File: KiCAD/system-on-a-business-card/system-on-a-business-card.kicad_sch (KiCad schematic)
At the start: 10 parts, among them J1 USB_C_Receptacle, SW1 SW_Push, U1 USBLC6-2SC6

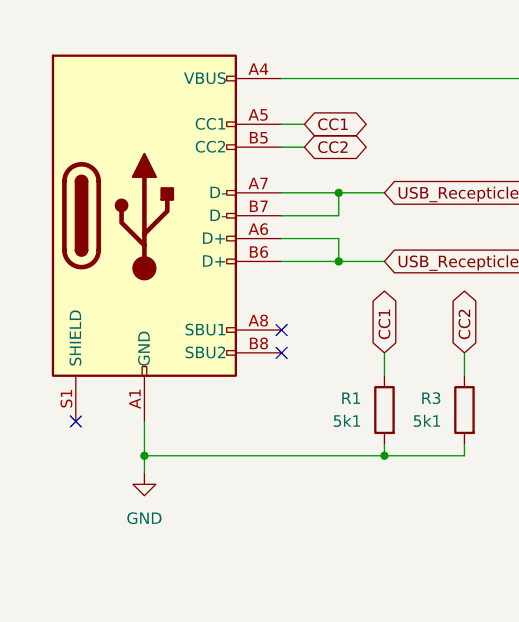
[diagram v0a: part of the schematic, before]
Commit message: fixed #12 connected OLED VDD pins to 3.3V power line
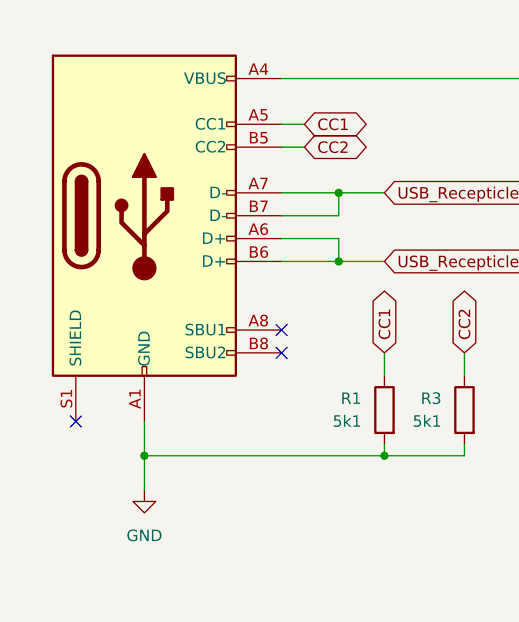
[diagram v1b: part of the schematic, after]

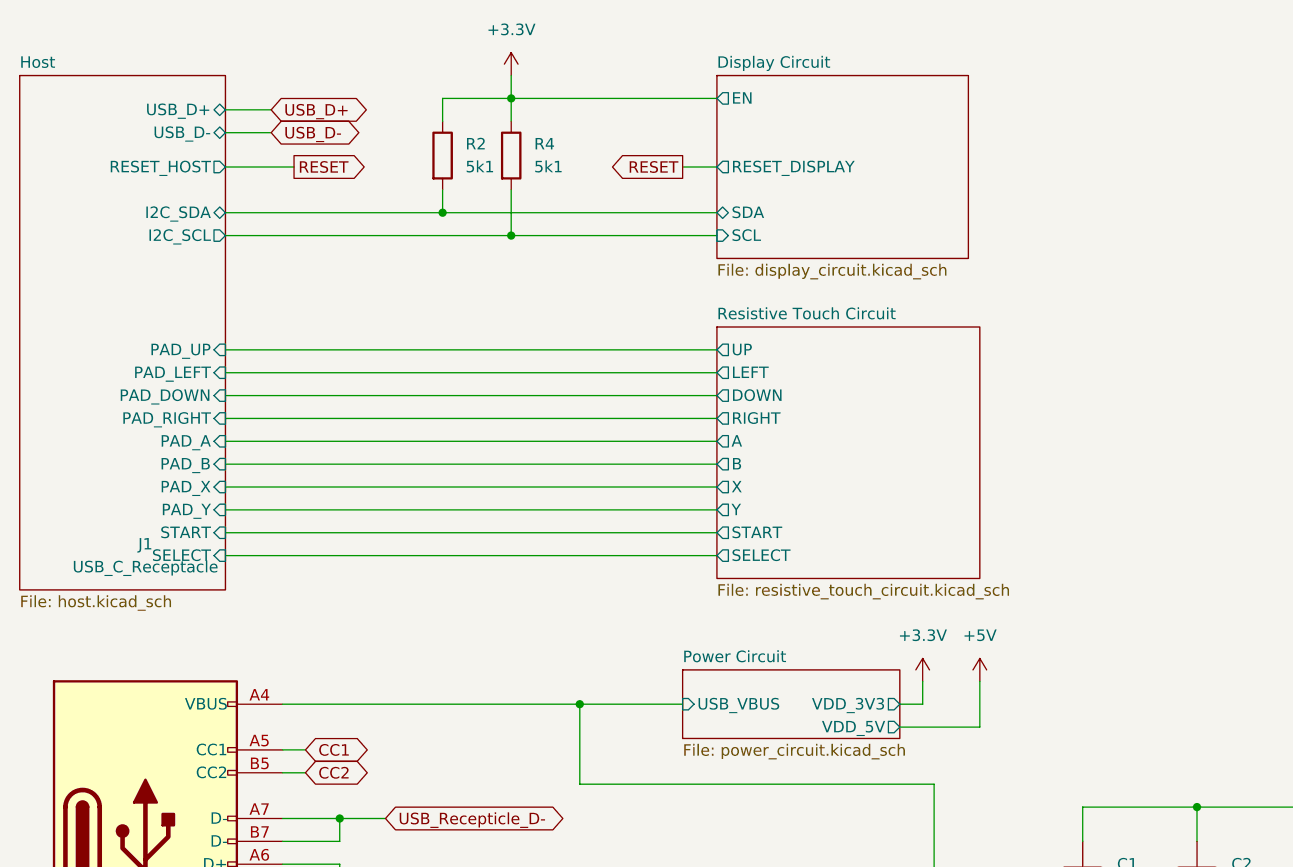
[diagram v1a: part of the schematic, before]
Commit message: #10: added buzzer, io-expander, removed transistors from resistive pad cirucit
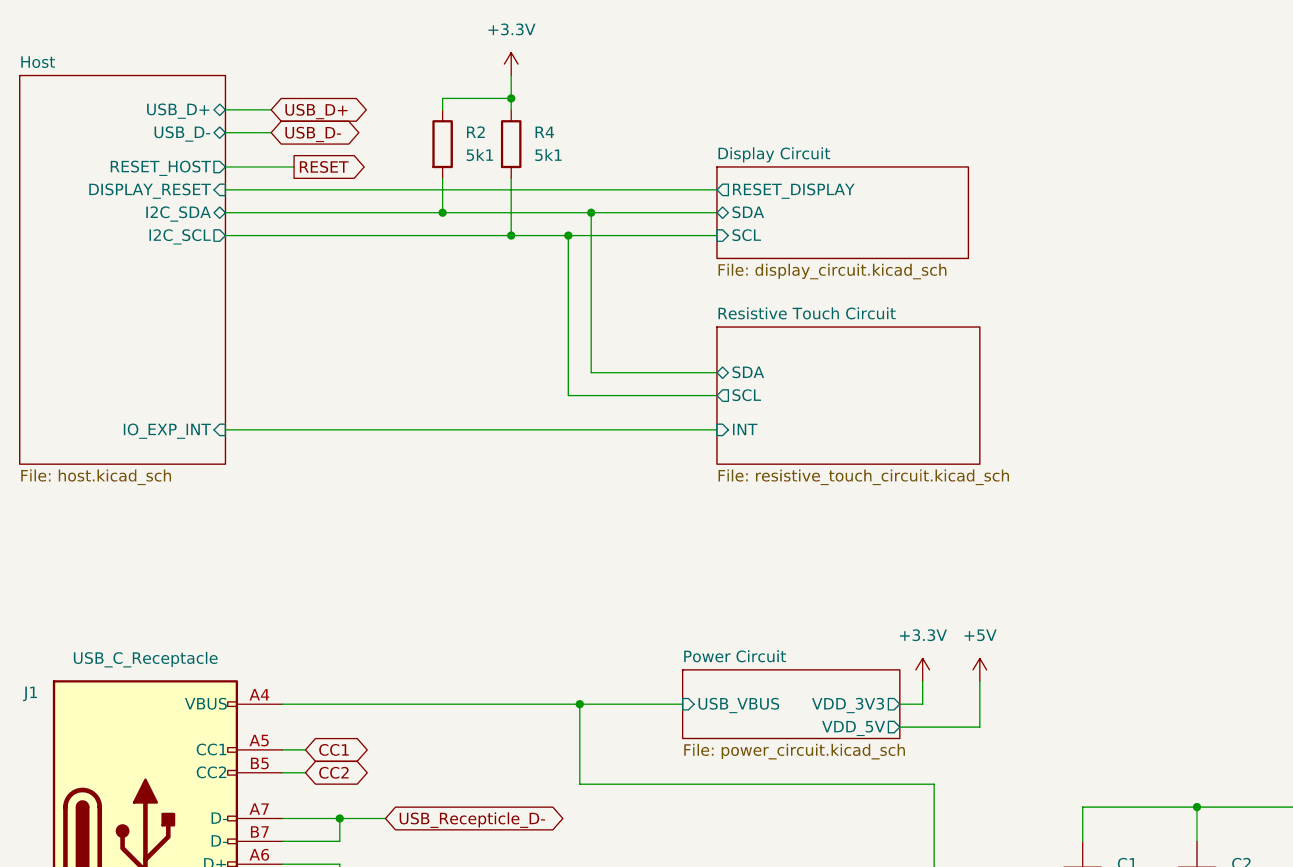
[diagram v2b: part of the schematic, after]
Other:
- sheet Display Circuit ports: added none; removed EN
- sheet Host ports: added DISPLAY_RESET, IO_EXP_INT; removed PAD_A, PAD_B, PAD_DOWN, PAD_LEFT, PAD_RIGHT, PAD_UP, PAD_X, PAD_Y, SELECT, START
- sheet Resistive Touch Circuit ports: added INT, SCL, SDA; removed A, B, DOWN, LEFT, RIGHT, SELECT, START, UP, X, Y
- moved on the sheet: R2, R4

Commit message: #10: removed on/off switch again, started working on layout
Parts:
- added J3: Conn_01x04_Socket, Connector_PinSocket_2.54mm:PinSocket_1x04_P2.54mm_Vertical, symbol Connector:Conn_01x04_Socket
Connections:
- net +3.3V: now also J3.4 (Pin_4)
- net GND: now also J3.1 (Pin_1)
- new net UART_RXD: J3.2 (Pin_2)
- new net UART_TXD: J3.3 (Pin_3)
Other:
- sheet Host ports: added UART_RXD, UART_TXD; removed none
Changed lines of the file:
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@@
+    (stroke (width 0) (type default))
+  )
+  (wire (pts (xy 195.58 73.66) (xy 195.58 71.12))
     (stroke (width 0) (type default))
   )
@@
     (stroke (width 0) (type default))
   )
+  (wire (pts (xy 195.58 68.58) (xy 199.39 68.58))
+    (stroke (width 0) (type default))
+  )
   (wire (pts (xy 143.51 154.94) (xy 143.51 157.48))
     (stroke (width 0) (type default))
@@
     (stroke (width 0) (type default))
   )
+  (wire (pts (xy 195.58 71.12) (xy 199.39 71.12))
+    (stroke (width 0) (type default))
+  )
   (wire (pts (xy 143.51 110.49) (xy 104.14 110.49))
     (stroke (width 0) (type default))
@@
     (stroke (width 0) (type default))
   )
+  (wire (pts (xy 195.58 63.5) (xy 199.39 63.5))
+    (stroke (width 0) (type default))
+  )
   (wire (pts (xy 64.77 38.1) (xy 69.85 38.1))
     (stroke (width 0) (type default))
@@
     (stroke (width 0) (type default))
   )
+  (wire (pts (xy 64.77 60.96) (xy 67.31 60.96))
+    (stroke (width 0) (type default))
+  )
   (wire (pts (xy 88.9 34.29) (xy 96.52 34.29))
     (stroke (width 0) (type default))
   )
+  (wire (pts (xy 64.77 58.42) (xy 67.31 58.42))
+    (stroke (width 0) (type default))
+  )
   (wire (pts (xy 172.72 113.03) (xy 186.69 113.03))
     (stroke (width 0) (type default))
@@
     (stroke (width 0) (type default))
   )
+  (wire (pts (xy 195.58 60.96) (xy 195.58 63.5))
+    (stroke (width 0) (type default))
+  )
   (wire (pts (xy 186.69 113.03) (xy 186.69 115.57))
     (stroke (width 0) (type default))
@@
     (stroke (width 0) (type default))
   )
+  (wire (pts (xy 195.58 66.04) (xy 199.39 66.04))
+    (stroke (width 0) (type default))
+  )
   (wire (pts (xy 154.94 147.32) (xy 153.67 147.32))
     (stroke (width 0) (type default))
@@
   (wire (pts (xy 172.72 128.27) (xy 186.69 128.27))
     (stroke (width 0) (type default))
+  )
+  (global_label "UART_RXD" (shape input) (at 195.58 68.58 180) (fields_autoplaced)
+    (effects (font (size 1.27 1.27)) (justify right))
+    (property "Intersheetrefs" "${INTERSHEET_REFS}" (at 183.221 68.58 0)
+      (effects (font (size 1.27 1.27)) (justify right) hide)
+    )
   )
   (global_label "USB_Recepticle_D-" (shape bidirectional) (at 154.94 142.24 0) (fields_autoplaced)
@@
     )
   )
+  (global_label "UART_TXD" (shape output) (at 195.58 66.04 180) (fields_autoplaced)
+    (effects (font (size 1.27 1.27)) (justify right))
+    (property "Intersheetrefs" "${INTERSHEET_REFS}" (at 183.5234 66.04 0)
+      (effects (font (size 1.27 1.27)) (justify right) hide)
+    )
+  )
   (global_label "CC2" (shape bidirectional) (at 91.44 132.08 90) (fields_autoplaced)
     (effects (font (size 1.27 1.27)) (justify left))
@@
     (effects (font (size 1.27 1.27)) (justify left))
     (property "Intersheetrefs" "${INTERSHEET_REFS}" (at 80.5483 41.8306 0)
+      (effects (font (size 1.27 1.27)) (justify left) hide)
+    )
+  )
+  (global_label "UART_RXD" (shape output) (at 67.31 60.96 0) (fields_autoplaced)
+    (effects (font (size 1.27 1.27)) (justify left))
+    (property "Intersheetrefs" "${INTERSHEET_REFS}" (at 79.669 60.96 0)
+      (effects (font (size 1.27 1.27)) (justify left) hide)
+    )
+  )
+  (global_label "UART_TXD" (shape input) (at 67.31 58.42 0) (fields_autoplaced)
+    (effects (font (size 1.27 1.27)) (justify left))
+    (property "Intersheetrefs" "${INTERSHEET_REFS}" (at 79.3666 58.42 0)
       (effects (font (size 1.27 1.27)) (justify left) hide)
     )
@@
     )
   )
+  (symbol (lib_id "power:GND") (at 195.58 73.66 0) (unit 1)
+    (in_bom yes) (on_board yes) (dnp no)
+    (property "Reference" "#PWR052" (at 195.58 80.01 0)
+      (effects (font (size 1.27 1.27)) hide)
+    )
+    (property "Value" "GND" (at 198.12 73.66 0)
+      (effects (font (size 1.27 1.27)))
+    )
+    (property "Footprint" "" (at 195.58 73.66 0)
+      (effects (font (size 1.27 1.27)) hide)
+    )
+    (property "Datasheet" "" (at 195.58 73.66 0)
+      (effects (font (size 1.27 1.27)) hide)
+    )
+    (pin "1")
+    (instances
+      (project "system-on-a-business-card"
+        (path "/49855302-2ecc-4f42-8bbd-b9c2e284f529"
+          (reference "#PWR052") (unit 1)
+        )
+      )
+    )
+  )
   (symbol (lib_id "power:+5V") (at 148.59 99.06 0) (unit 1)
     (in_bom yes) (on_board yes) (dnp no)
@@
     )
   )
+  (symbol (lib_id "Connector:Conn_01x04_Socket") (at 204.47 68.58 0) (mirror x) (unit 1)
+    (in_bom yes) (on_board yes) (dnp no)
+    (property "Reference" "J3" (at 205.74 68.58 0)
+      (effects (font (size 1.27 1.27)) (justify left))
+    )
+    (property "Value" "Conn_01x04_Socket" (at 205.74 66.04 0)
+      (effects (font (size 1.27 1.27)) (justify left))
+    )
+    (property "Footprint" "Connector_PinSocket_2.54mm:PinSocket_1x04_P2.54mm_Vertical" (at 204.47 68.58 0)
+      (effects (font (size 1.27 1.27)) hide)
+    )
+    (property "Datasheet" "~" (at 204.47 68.58 0)
+      (effects (font (size 1.27 1.27)) hide)
+    )
+    (pin "1")
+    (pin "2")
+    (pin "3")
+    (pin "4")
+    (instances
+      (project "system-on-a-business-card"
+        (path "/49855302-2ecc-4f42-8bbd-b9c2e284f529"
+          (reference "J3") (unit 1)
+        )
+      )
+    )
+  )
   (symbol (lib_id "power:+3.3V") (at 186.69 100.33 0) (unit 1)
     (in_bom yes) (on_board yes) (dnp no)
@@
         (path "/49855302-2ecc-4f42-8bbd-b9c2e284f529"
           (reference "#PWR07") (unit 1)
+        )
+      )
+    )
+  )
+  (symbol (lib_id "power:+3.3V") (at 195.58 60.96 0) (unit 1)
+    (in_bom yes) (on_board yes) (dnp no)
+    (property "Reference" "#PWR051" (at 195.58 64.77 0)
+      (effects (font (size 1.27 1.27)) hide)
+    )
+    (property "Value" "+3.3V" (at 195.58 55.88 0)
+      (effects (font (size 1.27 1.27)))
+    )
+    (property "Footprint" "" (at 195.58 60.96 0)
+      (effects (font (size 1.27 1.27)) hide)
+    )
+    (property "Datasheet" "" (at 195.58 60.96 0)
+      (effects (font (size 1.27 1.27)) hide)
+    )
+    (pin "1")
+    (instances
+      (project "system-on-a-business-card"
+        (path "/49855302-2ecc-4f42-8bbd-b9c2e284f529"
+          (reference "#PWR051") (unit 1)
         )
       )
@@
       (effects (font (size 1.27 1.27)) (justify right))
     )
+    (pin "UART_TXD" input (at 64.77 58.42 0)
+      (effects (font (size 1.27 1.27)) (justify right))
+    )
+    (pin "UART_RXD" output (at 64.77 60.96 0)
+      (effects (font (size 1.27 1.27)) (justify right))
+    )

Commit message: #10: started with routing
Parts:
- added FID1, FID2, FID3, FID4: Fiducial, Fiducial:Fiducial_1mm_Mask2mm, symbol Mechanical:Fiducial
- J3: footprint Connector_PinSocket_2.54mm:PinSocket_1x04_P2.54mm_Vertical -> Prj_connectors:solder_pads_4x1; now left out of the parts list
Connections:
- net UART_RXD: now also J3.3 (Pin_3); no longer J3.2 (Pin_2)
- net UART_TXD: now also J3.2 (Pin_2); no longer J3.3 (Pin_3)
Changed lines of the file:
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@@
     (stroke (width 0) (type default))
   )
-  (global_label "UART_RXD" (shape input) (at 195.58 68.58 180) (fields_autoplaced)
+  (global_label "UART_RXD" (shape input) (at 195.58 66.04 180) (fields_autoplaced)
     (effects (font (size 1.27 1.27)) (justify right))
-    (property "Intersheetrefs" "${INTERSHEET_REFS}" (at 183.221 68.58 0)
+    (property "Intersheetrefs" "${INTERSHEET_REFS}" (at 183.221 66.04 0)
       (effects (font (size 1.27 1.27)) (justify right) hide)
     )
@@
     )
   )
-  (global_label "UART_TXD" (shape output) (at 195.58 66.04 180) (fields_autoplaced)
+  (global_label "UART_TXD" (shape output) (at 195.58 68.58 180) (fields_autoplaced)
     (effects (font (size 1.27 1.27)) (justify right))
-    (property "Intersheetrefs" "${INTERSHEET_REFS}" (at 183.5234 66.04 0)
+    (property "Intersheetrefs" "${INTERSHEET_REFS}" (at 183.5234 68.58 0)
       (effects (font (size 1.27 1.27)) (justify right) hide)
     )
@@
     )
   )
+  (symbol (lib_id "Mechanical:Fiducial") (at 257.81 73.66 0) (unit 1)
+    (in_bom yes) (on_board yes) (dnp no) (fields_autoplaced)
+    (property "Reference" "FID3" (at 260.35 72.39 0)
+      (effects (font (size 1.27 1.27)) (justify left))
+    )
+    (property "Value" "Fiducial" (at 260.35 74.93 0)
+      (effects (font (size 1.27 1.27)) (justify left))
+    )
+    (property "Footprint" "Fiducial:Fiducial_1mm_Mask2mm" (at 257.81 73.66 0)
+      (effects (font (size 1.27 1.27)) hide)
+    )
+    (property "Datasheet" "~" (at 257.81 73.66 0)
+      (effects (font (size 1.27 1.27)) hide)
+    )
+    (instances
+      (project "system-on-a-business-card"
+        (path "/49855302-2ecc-4f42-8bbd-b9c2e284f529"
+          (reference "FID3") (unit 1)
+        )
+      )
+    )
+  )
   (symbol (lib_id "Switch:SW_Push") (at 186.69 120.65 90) (unit 1)
     (in_bom yes) (on_board yes) (dnp no)
@@
   )
   (symbol (lib_id "Connector:Conn_01x04_Socket") (at 204.47 68.58 0) (mirror x) (unit 1)
-    (in_bom yes) (on_board yes) (dnp no)
+    (in_bom no) (on_board yes) (dnp no)
     (property "Reference" "J3" (at 205.74 68.58 0)
       (effects (font (size 1.27 1.27)) (justify left))
@@
       (effects (font (size 1.27 1.27)) (justify left))
     )
-    (property "Footprint" "Connector_PinSocket_2.54mm:PinSocket_1x04_P2.54mm_Vertical" (at 204.47 68.58 0)
+    (property "Footprint" "Prj_connectors:solder_pads_4x1" (at 204.47 68.58 0)
       (effects (font (size 1.27 1.27)) hide)
     )
@@
     )
   )
+  (symbol (lib_id "Mechanical:Fiducial") (at 257.81 67.31 0) (unit 1)
+    (in_bom yes) (on_board yes) (dnp no) (fields_autoplaced)
+    (property "Reference" "FID2" (at 260.35 66.04 0)
+      (effects (font (size 1.27 1.27)) (justify left))
+    )
+    (property "Value" "Fiducial" (at 260.35 68.58 0)
+      (effects (font (size 1.27 1.27)) (justify left))
+    )
+    (property "Footprint" "Fiducial:Fiducial_1mm_Mask2mm" (at 257.81 67.31 0)
+      (effects (font (size 1.27 1.27)) hide)
+    )
+    (property "Datasheet" "~" (at 257.81 67.31 0)
+      (effects (font (size 1.27 1.27)) hide)
+    )
+    (instances
+      (project "system-on-a-business-card"
+        (path "/49855302-2ecc-4f42-8bbd-b9c2e284f529"
+          (reference "FID2") (unit 1)
+        )
+      )
+    )
+  )
   (symbol (lib_id "power:+3.3V") (at 142.24 99.06 0) (unit 1)
     (in_bom yes) (on_board yes) (dnp no)
@@
     )
   )
+  (symbol (lib_id "Mechanical:Fiducial") (at 257.81 60.96 0) (unit 1)
+    (in_bom yes) (on_board yes) (dnp no) (fields_autoplaced)
+    (property "Reference" "FID1" (at 260.35 59.69 0)
+      (effects (font (size 1.27 1.27)) (justify left))
+    )
+    (property "Value" "Fiducial" (at 260.35 62.23 0)
+      (effects (font (size 1.27 1.27)) (justify left))
+    )
+    (property "Footprint" "Fiducial:Fiducial_1mm_Mask2mm" (at 257.81 60.96 0)
+      (effects (font (size 1.27 1.27)) hide)
+    )
+    (property "Datasheet" "~" (at 257.81 60.96 0)
+      (effects (font (size 1.27 1.27)) hide)
+    )
+    (instances
+      (project "system-on-a-business-card"
+        (path "/49855302-2ecc-4f42-8bbd-b9c2e284f529"
+          (reference "FID1") (unit 1)
+        )
+      )
+    )
+  )
   (symbol (lib_id "power:+3.3V") (at 96.52 31.75 0) (unit 1)
     (in_bom yes) (on_board yes) (dnp no) (fields_autoplaced)
@@
         )
       )
+    )
+  )
+  (symbol (lib_id "Mechanical:Fiducial") (at 257.81 80.01 0) (unit 1)
+    (in_bom yes) (on_board yes) (dnp no) (fields_autoplaced)
+    (property "Reference" "FID4" (at 260.35 78.74 0)
+      (effects (font (size 1.27 1.27)) (justify left))
+    )
+    (property "Value" "Fiducial" (at 260.35 81.28 0)
+      (effects (font (size 1.27 1.27)) (justify left))
+    )
+    (property "Footprint" "Fiducial:Fiducial_1mm_Mask2mm" (at 257.81 80.01 0)
+      (effects (font (size 1.27 1.27)) hide)
+    )
+    (property "Datasheet" "~" (at 257.81 80.01 0)
+      (effects (font (size 1.27 1.27)) hide)
+    )
+    (instances
+      (project "system-on-a-business-card"
+        (path "/49855302-2ecc-4f42-8bbd-b9c2e284f529"
+          (reference "FID4") (unit 1)
+        )
+      )

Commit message: #10: added micro sd card
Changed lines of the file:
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@@
       (effects (font (size 1.27 1.27)) (justify left))
     )
-    (pin "INT" input (at 119.38 71.12 180)
+    (pin "INT" output (at 119.38 71.12 180)
       (effects (font (size 1.27 1.27)) (justify left))
     )

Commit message: #10: finished initial routing
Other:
- sheet Host ports: added SDcard_DET; removed none
- sheet Resistive Touch Circuit ports: added SDCard_DET; removed none
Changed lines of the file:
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@@
     (stroke (width 0) (type default))
   )
-  (wire (pts (xy 102.87 67.31) (xy 102.87 49.53))
+  (wire (pts (xy 102.87 64.77) (xy 102.87 49.53))
     (stroke (width 0) (type default))
   )
@@
     (stroke (width 0) (type default))
   )
-  (wire (pts (xy 105.41 64.77) (xy 105.41 46.99))
+  (wire (pts (xy 105.41 62.23) (xy 105.41 46.99))
     (stroke (width 0) (type default))
   )
@@
     (stroke (width 0) (type default))
   )
-  (wire (pts (xy 119.38 64.77) (xy 105.41 64.77))
+  (wire (pts (xy 119.38 62.23) (xy 105.41 62.23))
     (stroke (width 0) (type default))
   )
@@
     (stroke (width 0) (type default))
   )
-  (wire (pts (xy 119.38 67.31) (xy 102.87 67.31))
+  (wire (pts (xy 119.38 64.77) (xy 102.87 64.77))
     (stroke (width 0) (type default))
   )
   (wire (pts (xy 64.77 35.56) (xy 69.85 35.56))
+    (stroke (width 0) (type default))
+  )
+  (wire (pts (xy 64.77 68.58) (xy 119.38 68.58))
     (stroke (width 0) (type default))
   )
@@
       (effects (font (size 1.27 1.27)) (justify left top))
     )
-    (pin "SDA" bidirectional (at 119.38 64.77 180)
-      (effects (font (size 1.27 1.27)) (justify left))
-    )
-    (pin "SCL" output (at 119.38 67.31 180)
+    (pin "SDA" bidirectional (at 119.38 62.23 180)
+      (effects (font (size 1.27 1.27)) (justify left))
+    )
+    (pin "SCL" output (at 119.38 64.77 180)
       (effects (font (size 1.27 1.27)) (justify left))
     )
     (pin "INT" output (at 119.38 71.12 180)
+      (effects (font (size 1.27 1.27)) (justify left))
+    )
+    (pin "SDCard_DET" input (at 119.38 68.58 180)
       (effects (font (size 1.27 1.27)) (justify left))
     )
@@
       (effects (font (size 1.27 1.27)) (justify right))
     )
+    (pin "SDcard_DET" output (at 64.77 68.58 0)
+      (effects (font (size 1.27 1.27)) (justify right))
+    )
